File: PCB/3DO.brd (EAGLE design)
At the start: 58.5 x 61 mm, 7 parts, among them U1 SN74AHCT125N, U2 SN74AHCT125N

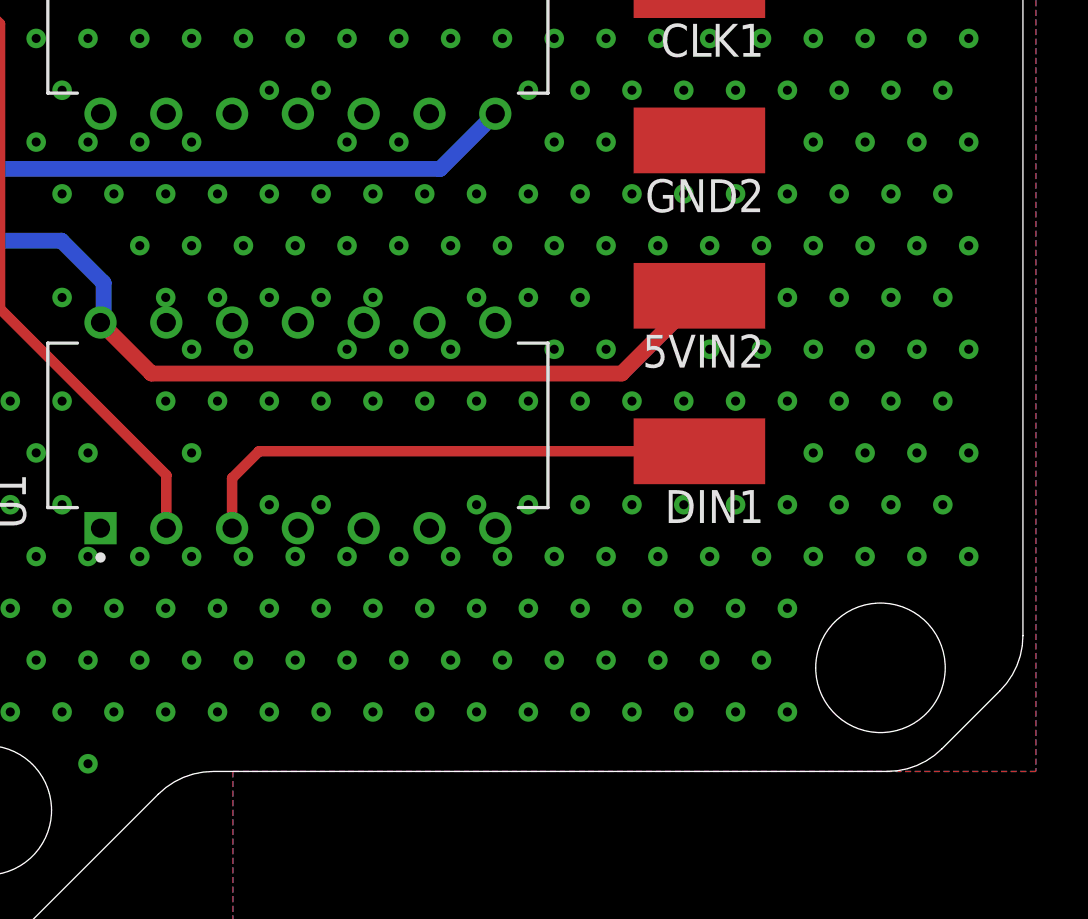
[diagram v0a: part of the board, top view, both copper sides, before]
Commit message: PCB Updates/New Additions
All existing PCBs had silkscreen updates and NES, Virtual Boy, PSX/PS2, Nintendo 64, Saturn have been added.
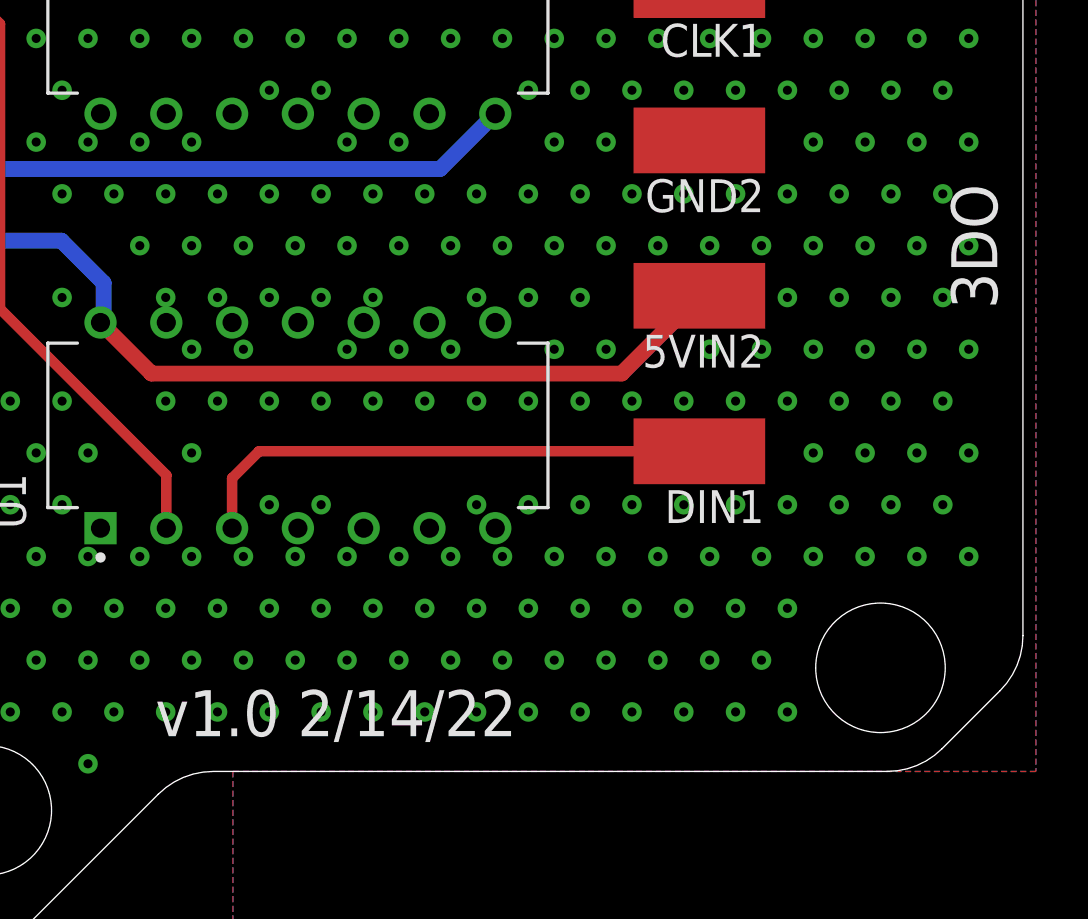
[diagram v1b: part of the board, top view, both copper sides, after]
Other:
- board text added: "3DO"
- board text added: "v1.0 2/14/22"
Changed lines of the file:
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@@
 <hole x="18.49" y="53.14" drill="5"/>
 <hole x="18.49" y="8.14" drill="5"/>
+<text x="57.5" y="27.5" size="1.778" layer="21" rot="R90">3DO</text>
+<text x="25" y="11" size="1.778" layer="21">v1.0 2/14/22</text>
 </plain>
 <attributes>

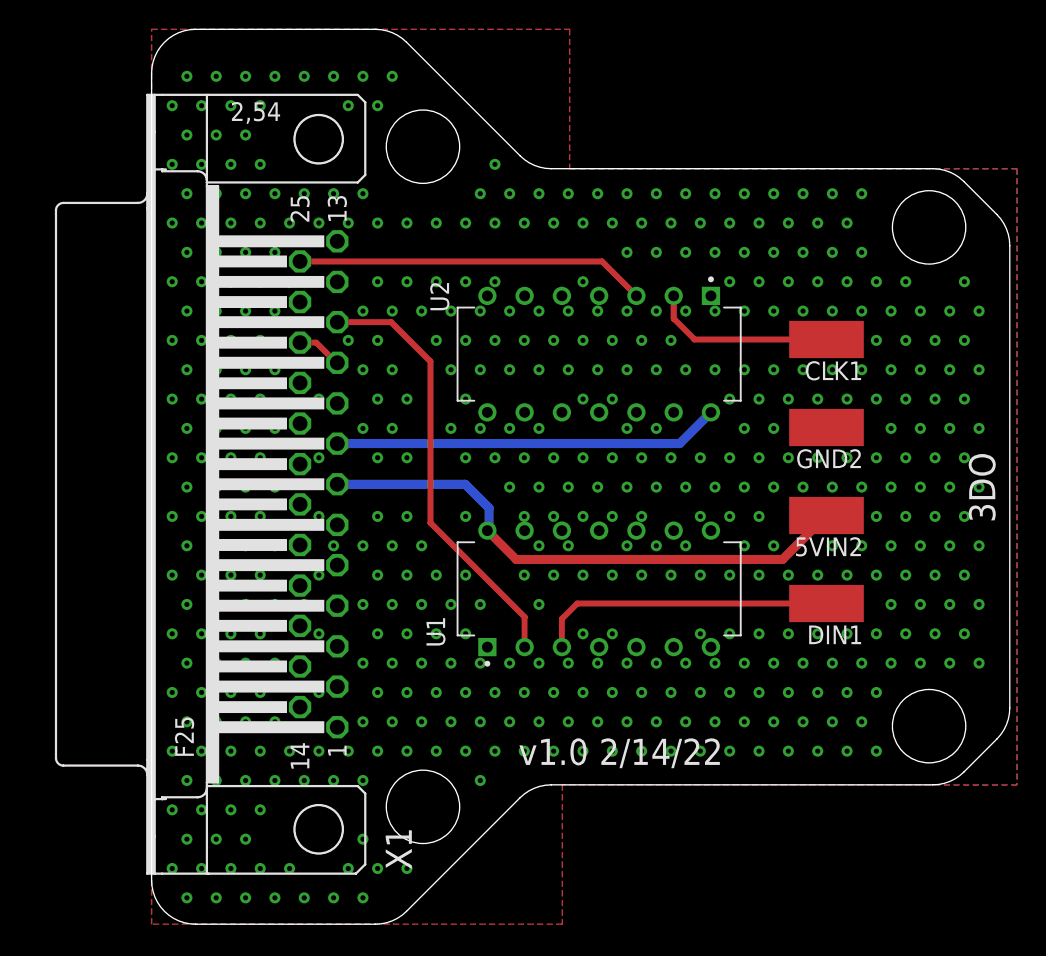
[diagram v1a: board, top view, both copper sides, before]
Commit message: PCB Update for better Housing Fit
All the PCBs were updated for better housing fitment.

Common Changes across all PCBs:
1. All Aux PCBs are now the exact same size.  (there was a .1mm-.5mm Variance previous)
2. All Aux PCBs Mounting holes are in the same location (there was a .05mm-.1mm Variance previous)
3. The DB25 has been moved 1.2mm close to the edge of the PCB for better connection when in the housing.

PCB Specific Updates:
3DO - Rename Pads (Removed trailing numbers), Flipped U2 to match U1, Moved U1 & U2 to same coordinates as other 2 Component PCBs in collection.

PCE & NES- Moved U1 & U2 to same coordinates as other 2 Component PCBs in collection.

PS2/PSX & Saturn - Added Notch on back edge of PCB for access for wires that need to attach to bottom layer of PCB.

All Gerbers have been updated.

New PCBs have been ordered for testing.
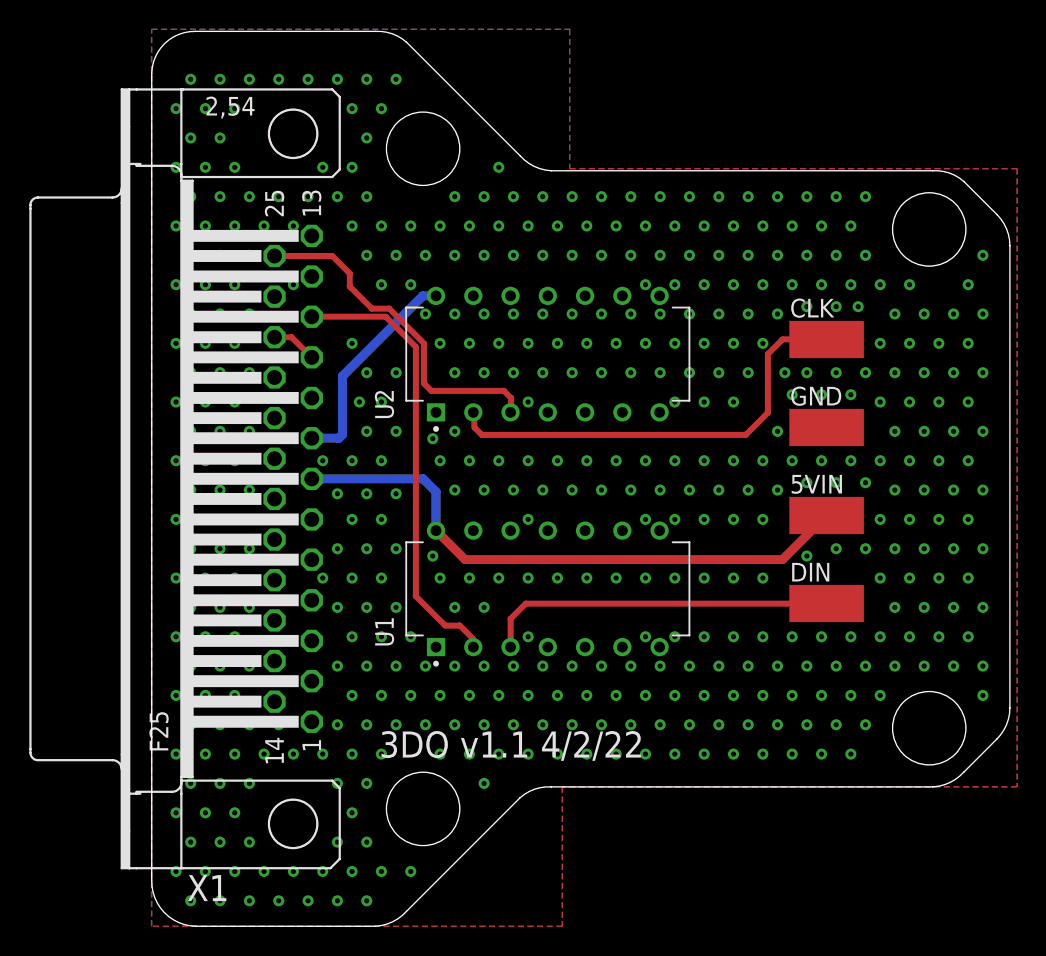
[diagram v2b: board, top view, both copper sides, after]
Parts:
- moved U1 3.50 mm to (27.0, 23.0)
- moved U2 3.50 mm to (27.0, 39.0), turned to 90 degrees
- moved X1 1.78 mm to (9.64, 30.5)
- renumbered 5VIN2 to 5VIN, CLK1 to CLK, DIN1 to DIN, GND2 to GND
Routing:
- net CLK: track 12.6 -> 30.3 mm
- net 3V3IN: track 26.4 -> 14.8 mm
- net DIN: track 20.4 -> 23.9 mm
- net 5VIN: track 37.8 -> 40.2 mm
- net IO21: track 29.6 -> 30.6 mm
- net IO22: track 23.9 -> 23.3 mm
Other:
- outline, holes or cut-outs redrawn
- board text added: "3DO v1.1 4/2/22"
- board text removed: "3DO"
- board text removed: "v1.0 2/14/22"

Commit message: Added exposed GND plane at DB25 anchors
All PCBs have been update to have exposed GND plane pads for the DB25 anchor points.

This resolves Issue 54
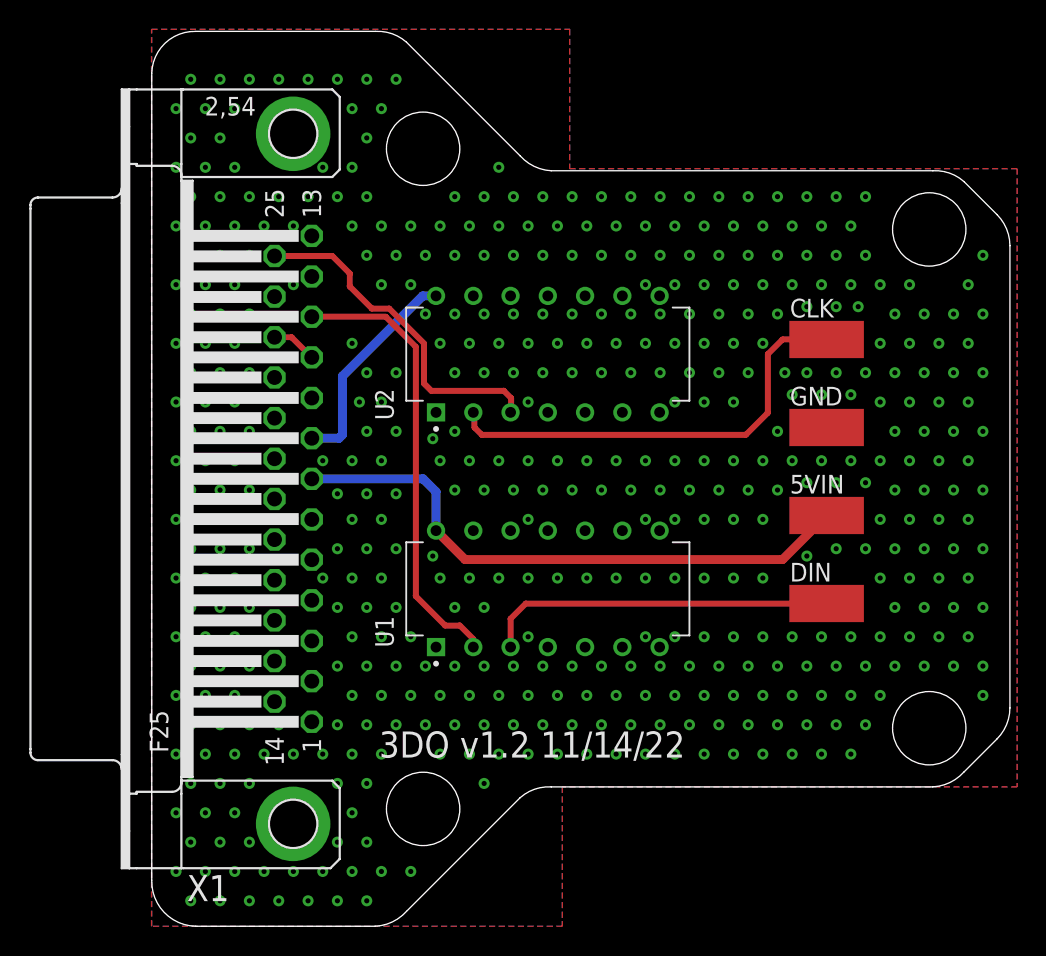
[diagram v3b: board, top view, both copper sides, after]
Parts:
- X1: device SparkFun-Retired:F25H -> SparkFun-Retired:F25HP
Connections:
- net GND: now also X1.GND1, X1.GND2
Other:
- board text added: "3DO v1.2 11/14/22"
- board text removed: "3DO v1.1 4/2/22"
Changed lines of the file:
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@@
 <drawing>
 <settings>
-<setting alwaysvectorfont="no"/>
+<setting alwaysvectorfont="yes"/>
 <setting verticaltext="up"/>
 </settings>
@@
 <hole x="18.5" y="53" drill="5"/>
 <hole x="18.5" y="8" drill="5"/>
-<text x="15.5" y="11.5" size="1.778" layer="21">3DO v1.1 4/2/22</text>
+<text x="15.5" y="11.5" size="1.778" layer="21">3DO v1.2 11/14/22</text>
 </plain>
 <attributes>
@@
 <attribute name="PURCHASE-URL" value="https://pricing.snapeda.com/search/part/SN74AHCT125N/?ref=eda" x="65.1" y="63.13" size="1.778" layer="27" rot="R90" display="off"/>
 </element>
-<element name="X1" library="SparkFun-Retired" package="F25H" value="" x="9.64" y="30.5" smashed="yes" rot="R90">
+<element name="X1" library="SparkFun-Retired" package="F25HP" value="" x="9.64" y="30.5" smashed="yes" rot="R90">
 <attribute name="NAME" x="5.289" y="3.49" size="1.778" layer="25" ratio="10" rot="R180"/>
 <attribute name="VALUE" x="-4.33" y="22.118" size="1.778" layer="27" ratio="10" rot="R90"/>
@@
 <signals>
 <signal name="GND">
-<contactref element="X1" pad="15"/>
-<contactref element="X1" pad="16"/>
-<contactref element="X1" pad="17"/>
-<contactref element="X1" pad="9"/>
-<contactref element="X1" pad="6"/>
-<contactref element="X1" pad="2"/>
-<contactref element="X1" pad="5"/>
-<contactref element="X1" pad="4"/>
-<contactref element="X1" pad="3"/>
 <contactref element="U2" pad="4"/>
 <contactref element="U2" pad="10"/>
@@
 <via x="55.6568" y="43.735840625" extent="1-16" drill="0.35"/>
 <via x="56.6568" y="45.735840625" extent="1-16" drill="0.35"/>
+<contactref element="X1" pad="15"/>
+<contactref element="X1" pad="16"/>
+<contactref element="X1" pad="17"/>
+<contactref element="X1" pad="9"/>
+<contactref element="X1" pad="6"/>
+<contactref element="X1" pad="2"/>
+<contactref element="X1" pad="5"/>
+<contactref element="X1" pad="4"/>
+<contactref element="X1" pad="3"/>
+<contactref element="X1" pad="GND2"/>
+<contactref element="X1" pad="GND1"/>
 </signal>
 <signal name="5VIN">

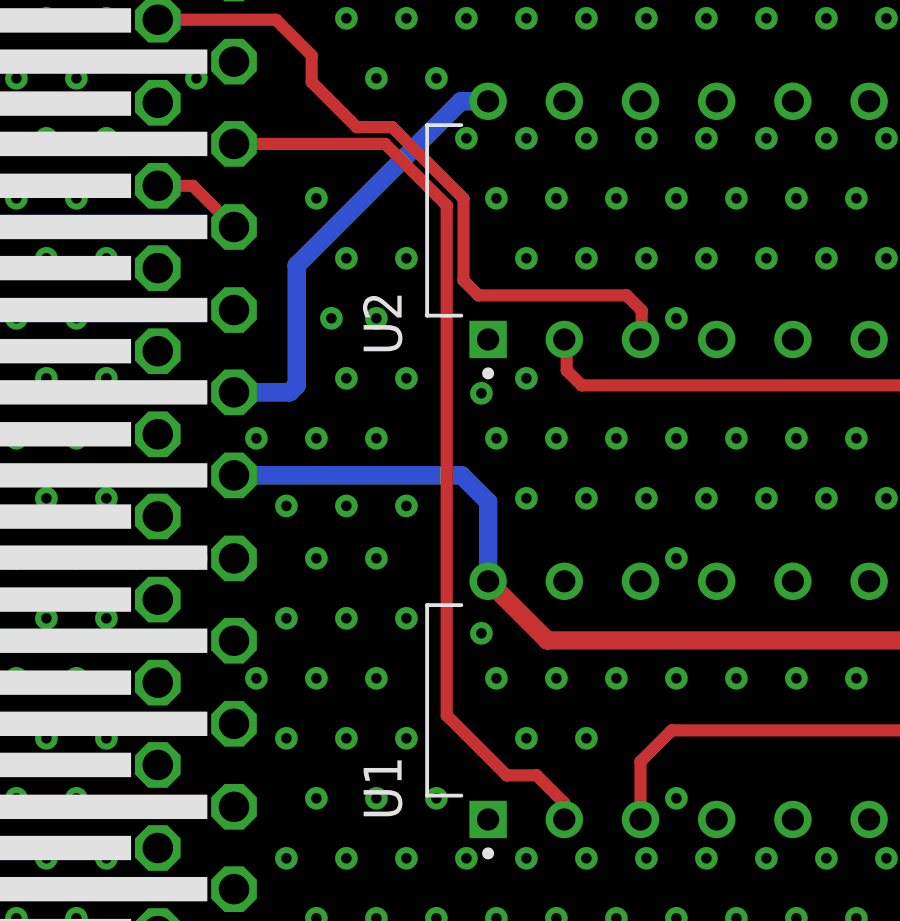
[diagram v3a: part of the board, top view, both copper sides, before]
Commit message: Silkscreen Update, Library Add, Datasheet Add
Updated the silkscreen on all PCBs that used the SN74 components as there was not orientation marker on the silkscreen.

Added Modified SN74 libraries and VB Cable Pinout image
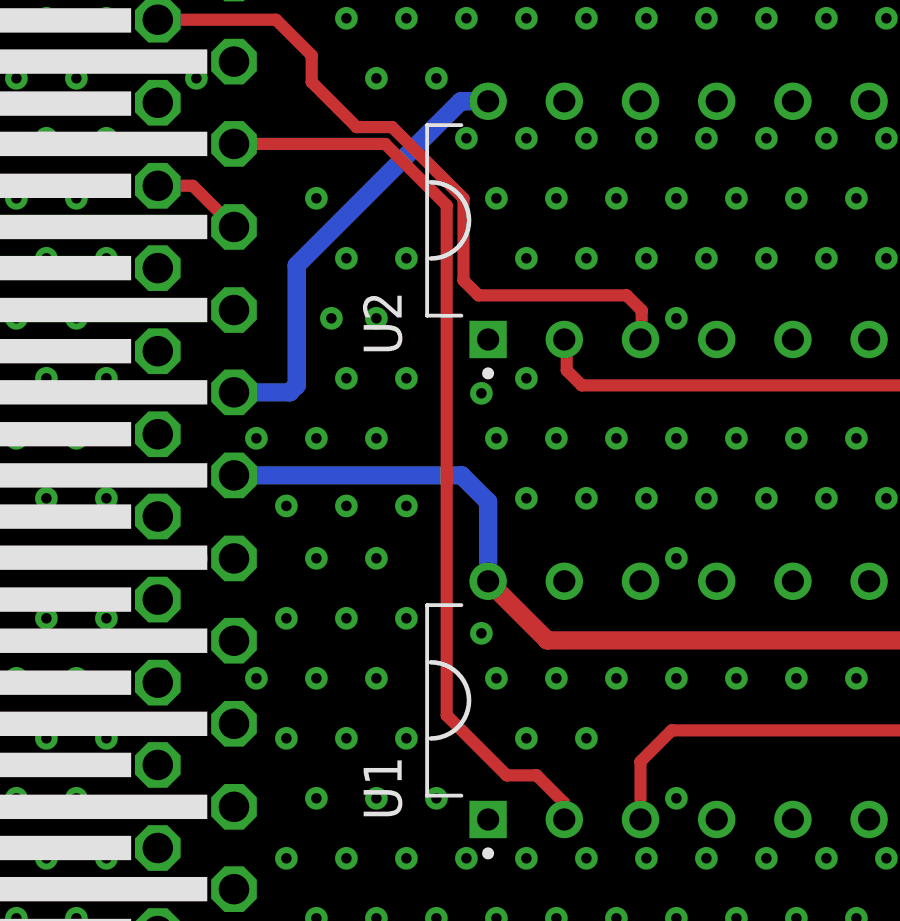
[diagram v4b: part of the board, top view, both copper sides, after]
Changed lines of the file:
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@@
 <drawing>
 <settings>
-<setting alwaysvectorfont="yes"/>
+<setting alwaysvectorfont="no"/>
 <setting verticaltext="up"/>
 </settings>
